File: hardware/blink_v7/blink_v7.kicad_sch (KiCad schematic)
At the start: 94 parts, among them J1 Conn_01x02, J14 Conn_02x16_Odd_Even, J5 Conn_01x04_Pin, J6 Conn_01x04_Pin, J7 Conn_01x06_Pin, J8 Conn_01x06, J9 USB_C_Receptacle, SW1 MK-12C02-G025, U1 AMS1117-3.3, U3 M24C02-RMN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

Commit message: start to add push button switch
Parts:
- added SW2, SW3, SW4: SW_SPDT, Button_Switch_THT:SW_Push_1P2T_Vertical_E-Switch_800UDP8P1A1M6, symbol Switch:SW_SPDT
- C27: JLCPCB Part # (none) -> C1525; JLCPCB# C1525 -> (none)
- C28, C29: JLCPCB Part # (none) -> C23733; JLCPCB# C23733 -> (none)
- D1: JLCPCB Part # (none) -> C130114; JLCPCB# C130114 -> (none)
- D2, D3: JLCPCB Part # (none) -> C191023; JLCPCB# C191023 -> (none)
- J9: JLCPCB Part # (none) -> C165948; JLCPCB# C165948 -> (none)
- R21, R22: JLCPCB Part # (none) -> C25905; JLCPCB# C25905 -> (none)
- R27: JLCPCB Part # C11702 -> C21190
- S1, S2: JLCPCB Part # (none) -> C266189
- U7: JLCPCB Part # (none) -> C84681; JLCPCB# C84681 -> (none)
- U8: JLCPCB Part # (none) -> C2827693; JLCPCB# C2827693 -> (none)
- U9: JLCPCB Part # (none) -> C424093; JLCPCB# C424093 -> (none)
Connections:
- net BTN1: now also SW2.2 (B)
- net GND: now also SW2.3 (C), SW3.3 (C), SW4.3 (C)

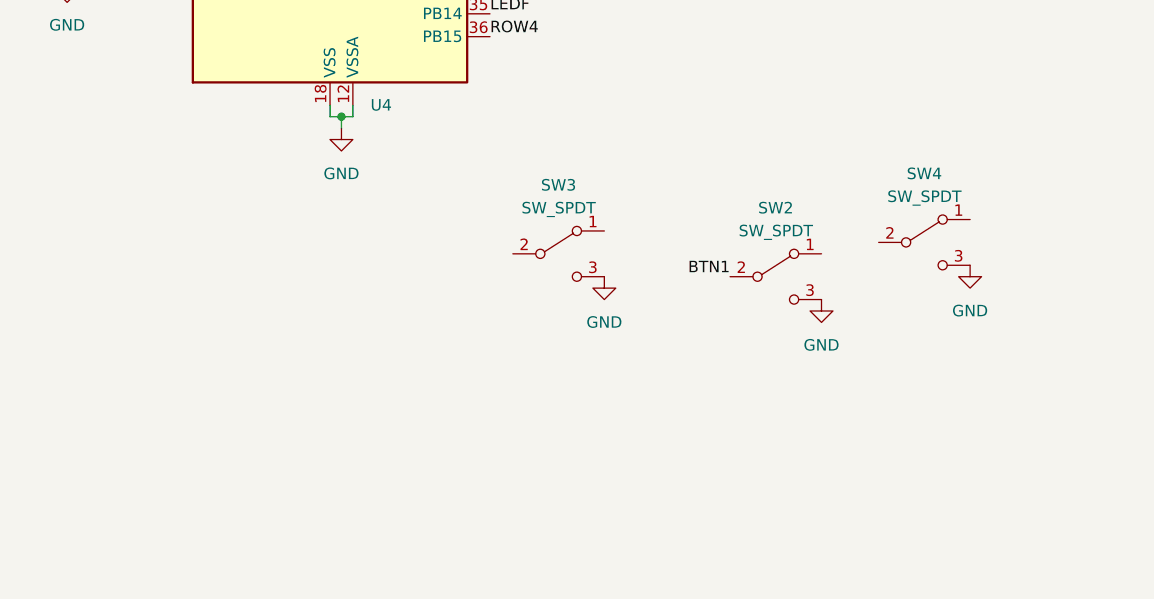
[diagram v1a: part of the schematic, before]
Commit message: wire up new switches
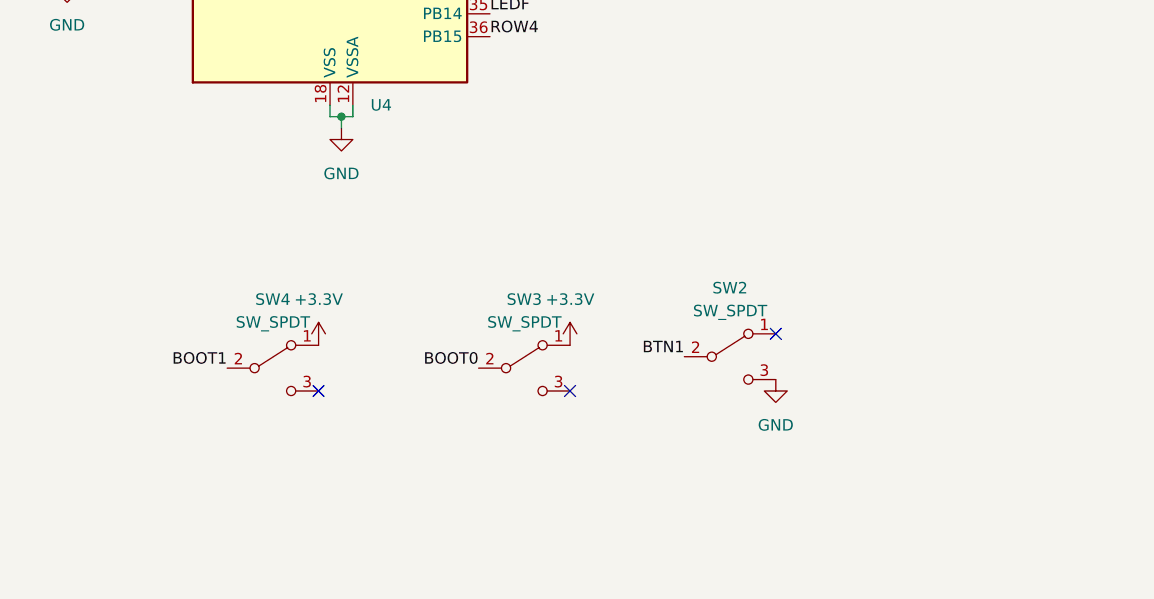
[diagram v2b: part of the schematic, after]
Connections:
- net +3.3V: now also SW3.1 (A), SW4.1 (A)
- net BOOT0: now also SW3.2 (B)
- net BOOT1: now also SW4.2 (B)
- net GND: no longer SW3.3 (C), SW4.3 (C)
- no-connect marks 21 -> 24
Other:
- moved on the sheet: SW2, SW3, SW4
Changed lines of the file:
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@@
   (junction (at 271.78 245.11) (diameter 0) (color 0 0 0 0)
   )
+  (no_connect (at 274.32 147.32))
   (no_connect (at 54.61 63.5))
   (no_connect (at 340.36 181.61))
+  (no_connect (at 223.52 153.67))
   (no_connect (at 389.89 184.15))
+  (no_connect (at 251.46 153.67))
   (no_connect (at 389.89 176.53))
   (no_connect (at 389.89 189.23))
@@
     (effects (font (size 1.27 1.27)) (justify left bottom))
   )
+  (label "BOOT0" (at 241.3 151.13 180) (fields_autoplaced)
+    (effects (font (size 1.27 1.27)) (justify right bottom))
+  )
   (label "SYNC_IN2" (at 207.01 71.12 180) (fields_autoplaced)
     (effects (font (size 1.27 1.27)) (justify right bottom))
@@
     (effects (font (size 1.27 1.27)) (justify left bottom))
   )
+  (label "BOOT1" (at 213.36 151.13 180) (fields_autoplaced)
+    (effects (font (size 1.27 1.27)) (justify right bottom))
+  )
   (label "USB_DTR" (at 309.88 196.85 0) (fields_autoplaced)
     (effects (font (size 1.27 1.27)) (justify left bottom))
@@
     (effects (font (size 1.27 1.27)) (justify left bottom))
   )
-  (label "BTN1" (at 269.24 140.97 180) (fields_autoplaced)
+  (label "BTN1" (at 264.16 149.86 180) (fields_autoplaced)
     (effects (font (size 1.27 1.27)) (justify right bottom))
   )
@@
     )
   )
-  (symbol (lib_id "Switch:SW_SPDT") (at 290.83 137.16 0) (unit 1)
+  (symbol (lib_id "Switch:SW_SPDT") (at 218.44 151.13 0) (unit 1)
     (in_bom yes) (on_board yes) (dnp no) (fields_autoplaced)
-    (property "Reference" "SW4" (at 290.83 129.54 0)
+    (property "Reference" "SW4" (at 218.44 143.51 0)
       (effects (font (size 1.27 1.27)))
     )
-    (property "Value" "SW_SPDT" (at 290.83 132.08 0)
+    (property "Value" "SW_SPDT" (at 218.44 146.05 0)
       (effects (font (size 1.27 1.27)))
     )
-    (property "Footprint" "Button_Switch_THT:SW_Push_1P2T_Vertical_E-Switch_800UDP8P1A1M6" (at 290.83 137.16 0)
+    (property "Footprint" "Button_Switch_THT:SW_Push_1P2T_Vertical_E-Switch_800UDP8P1A1M6" (at 218.44 151.13 0)
       (effects (font (size 1.27 1.27)) hide)
     )
-    (property "Datasheet" "~" (at 290.83 137.16 0)
+    (property "Datasheet" "~" (at 218.44 151.13 0)
       (effects (font (size 1.27 1.27)) hide)
     )
-    (property "JLCPCB Part #" "C273412" (at 290.83 137.16 0)
+    (property "JLCPCB Part #" "C273412" (at 218.44 151.13 0)
       (effects (font (size 1.27 1.27)) hide)
     )
@@
     )
   )
+  (symbol (lib_id "power:+3.3V") (at 223.52 148.59 0) (unit 1)
+    (in_bom yes) (on_board yes) (dnp no) (fields_autoplaced)
+    (property "Reference" "#PWR076" (at 223.52 152.4 0)
+      (effects (font (size 1.27 1.27)) hide)
+    )
+    (property "Value" "+3.3V" (at 223.52 143.51 0)
+      (effects (font (size 1.27 1.27)))
+    )
+    (property "Footprint" "" (at 223.52 148.59 0)
+      (effects (font (size 1.27 1.27)) hide)
+    )
+    (property "Datasheet" "" (at 223.52 148.59 0)
+      (effects (font (size 1.27 1.27)) hide)
+    )
+    (pin "1")
+    (instances
+      (project "blink_v7"
+        (path "/bd4d3b9a-07c1-4a53-9c94-2893f3e869d4"
+          (reference "#PWR076") (unit 1)
+        )
+      )
+    )
+  )
   (symbol (lib_id "Connector_Generic:Conn_01x06") (at 125.73 87.63 180) (unit 1)
     (in_bom yes) (on_board yes) (dnp no) (fields_autoplaced)
@@
     )
   )
-  (symbol (lib_id "power:GND") (at 279.4 143.51 0) (unit 1)
+  (symbol (lib_id "power:GND") (at 274.32 152.4 0) (unit 1)
     (in_bom yes) (on_board yes) (dnp no) (fields_autoplaced)
-    (property "Reference" "#PWR032" (at 279.4 149.86 0)
+    (property "Reference" "#PWR032" (at 274.32 158.75 0)
       (effects (font (size 1.27 1.27)) hide)
     )
-    (property "Value" "GND" (at 279.4 148.59 0)
+    (property "Value" "GND" (at 274.32 157.48 0)
       (effects (font (size 1.27 1.27)))
     )
-    (property "Footprint" "" (at 279.4 143.51 0)
+    (property "Footprint" "" (at 274.32 152.4 0)
       (effects (font (size 1.27 1.27)) hide)
     )
-    (property "Datasheet" "" (at 279.4 143.51 0)
+    (property "Datasheet" "" (at 274.32 152.4 0)
       (effects (font (size 1.27 1.27)) hide)
     )
@@
     )
   )
-  (symbol (lib_id "Switch:SW_SPDT") (at 250.19 138.43 0) (unit 1)
+  (symbol (lib_id "Switch:SW_SPDT") (at 246.38 151.13 0) (unit 1)
     (in_bom yes) (on_board yes) (dnp no) (fields_autoplaced)
-    (property "Reference" "SW3" (at 250.19 130.81 0)
+    (property "Reference" "SW3" (at 246.38 143.51 0)
       (effects (font (size 1.27 1.27)))
     )
-    (property "Value" "SW_SPDT" (at 250.19 133.35 0)
+    (property "Value" "SW_SPDT" (at 246.38 146.05 0)
       (effects (font (size 1.27 1.27)))
     )
-    (property "Footprint" "Button_Switch_THT:SW_Push_1P2T_Vertical_E-Switch_800UDP8P1A1M6" (at 250.19 138.43 0)
+    (property "Footprint" "Button_Switch_THT:SW_Push_1P2T_Vertical_E-Switch_800UDP8P1A1M6" (at 246.38 151.13 0)
       (effects (font (size 1.27 1.27)) hide)
     )
-    (property "Datasheet" "~" (at 250.19 138.43 0)
+    (property "Datasheet" "~" (at 246.38 151.13 0)
       (effects (font (size 1.27 1.27)) hide)
     )
-    (property "JLCPCB Part #" "C273412" (at 250.19 138.43 0)
+    (property "JLCPCB Part #" "C273412" (at 246.38 151.13 0)
       (effects (font (size 1.27 1.27)) hide)
     )
@@
     )
   )
+  (symbol (lib_id "power:+3.3V") (at 251.46 148.59 0) (unit 1)
+    (in_bom yes) (on_board yes) (dnp no) (fields_autoplaced)
+    (property "Reference" "#PWR077" (at 251.46 152.4 0)
+      (effects (font (size 1.27 1.27)) hide)
+    )
+    (property "Value" "+3.3V" (at 251.46 143.51 0)
+      (effects (font (size 1.27 1.27)))
+    )
+    (property "Footprint" "" (at 251.46 148.59 0)
+      (effects (font (size 1.27 1.27)) hide)
+    )
+    (property "Datasheet" "" (at 251.46 148.59 0)
+      (effects (font (size 1.27 1.27)) hide)
+    )
+    (pin "1")
+    (instances
+      (project "blink_v7"
+        (path "/bd4d3b9a-07c1-4a53-9c94-2893f3e869d4"
+          (reference "#PWR077") (unit 1)
+        )
+      )
+    )
+  )
   (symbol (lib_id "Device:C") (at 326.39 166.37 0) (mirror y) (unit 1)
     (in_bom yes) (on_board yes) (dnp no)
@@
     )
   )
-  (symbol (lib_id "power:GND") (at 295.91 139.7 0) (unit 1)
-    (in_bom yes) (on_board yes) (dnp no) (fields_autoplaced)
-    (property "Reference" "#PWR075" (at 295.91 146.05 0)
-      (effects (font (size 1.27 1.27)) hide)
-    )
-    (property "Value" "GND" (at 295.91 144.78 0)
-      (effects (font (size 1.27 1.27)))
-    )
-    (property "Footprint" "" (at 295.91 139.7 0)
-      (effects (font (size 1.27 1.27)) hide)
-    )
-    (property "Datasheet" "" (at 295.91 139.7 0)
-      (effects (font (size 1.27 1.27)) hide)
-    )
-    (pin "1")
-    (instances
-      (project "blink_v7"
-        (path "/bd4d3b9a-07c1-4a53-9c94-2893f3e869d4"
-          (reference "#PWR075") (unit 1)
-        )
-      )
-    )
-  )
   (symbol (lib_id "Device:R_Small_US") (at 323.85 105.41 0) (unit 1)
     (in_bom yes) (on_board yes) (dnp no)
@@
     )
   )
-  (symbol (lib_id "Switch:SW_SPDT") (at 274.32 140.97 0) (unit 1)
+  (symbol (lib_id "Switch:SW_SPDT") (at 269.24 149.86 0) (unit 1)
     (in_bom yes) (on_board yes) (dnp no) (fields_autoplaced)
-    (property "Reference" "SW2" (at 274.32 133.35 0)
+    (property "Reference" "SW2" (at 269.24 142.24 0)
       (effects (font (size 1.27 1.27)))
     )
-    (property "Value" "SW_SPDT" (at 274.32 135.89 0)
+    (property "Value" "SW_SPDT" (at 269.24 144.78 0)
       (effects (font (size 1.27 1.27)))
     )
-    (property "Footprint" "Button_Switch_THT:SW_Push_1P2T_Vertical_E-Switch_800UDP8P1A1M6" (at 274.32 140.97 0)
+    (property "Footprint" "Button_Switch_THT:SW_Push_1P2T_Vertical_E-Switch_800UDP8P1A1M6" (at 269.24 149.86 0)
       (effects (font (size 1.27 1.27)) hide)
     )
-    (property "Datasheet" "~" (at 274.32 140.97 0)
+    (property "Datasheet" "~" (at 269.24 149.86 0)
       (effects (font (size 1.27 1.27)) hide)
     )
-    (property "JLCPCB Part #" "C273412" (at 274.32 140.97 0)
+    (property "JLCPCB Part #" "C273412" (at 269.24 149.86 0)
       (effects (font (size 1.27 1.27)) hide)
     )
@@
         )
       )
-    )
-  )
-  (symbol (lib_id "power:GND") (at 255.27 140.97 0) (unit 1)
-    (in_bom yes) (on_board yes) (dnp no) (fields_autoplaced)
-    (property "Reference" "#PWR04" (at 255.27 147.32 0)
-      (effects (font (size 1.27 1.27)) hide)
-    )
-    (property "Value" "GND" (at 255.27 146.05 0)
-      (effects (font (size 1.27 1.27)))
-    )
-    (property "Footprint" "" (at 255.27 140.97 0)
-      (effects (font (size 1.27 1.27)) hide)
-    )
-    (property "Datasheet" "" (at 255.27 140.97 0)
-      (effects (font (size 1.27 1.27)) hide)
-    )
-    (pin "1")
-    (instances
-      (project "blink_v7"
-        (path "/bd4d3b9a-07c1-4a53-9c94-2893f3e869d4"
-          (reference "#PWR04") (unit 1)
-        )
-      )

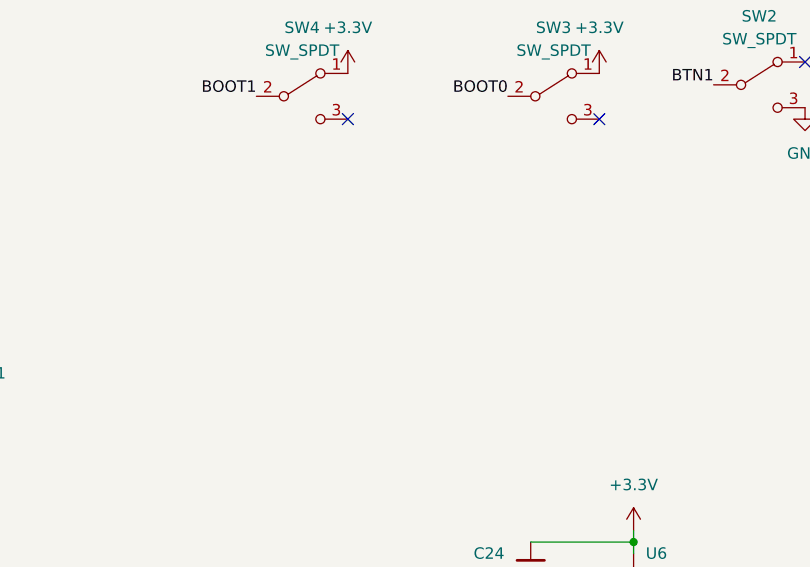
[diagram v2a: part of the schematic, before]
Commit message: start moving to new push switch
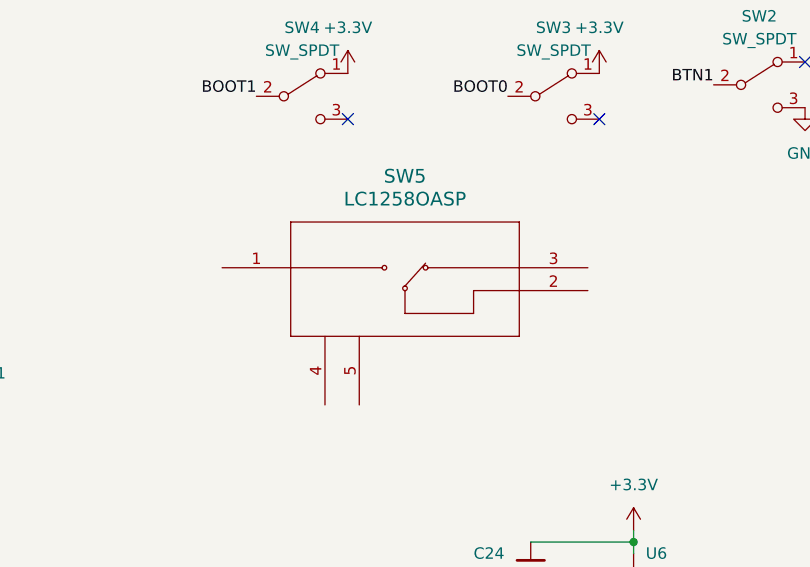
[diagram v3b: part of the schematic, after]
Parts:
- added SW5: LC1258OASP, blinky_footprints:LC1258OASP, symbol blinky:LC1258OASP
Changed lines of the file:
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@@
+    )
+  )
+  (symbol (lib_id "blinky:LC1258OASP") (at 209.55 170.18 0) (unit 1)
+    (in_bom yes) (on_board yes) (dnp no) (fields_autoplaced)
+    (property "Reference" "SW5" (at 229.87 160.02 0)
+      (effects (font (size 1.524 1.524)))
+    )
+    (property "Value" "LC1258OASP" (at 229.87 162.56 0)
+      (effects (font (size 1.524 1.524)))
+    )
+    (property "Footprint" "blinky_footprints:LC1258OASP" (at 229.87 176.53 0)
+      (effects (font (size 1.27 1.27) italic) hide)
+    )
+    (property "Datasheet" "" (at 209.55 170.18 0)
+      (effects (font (size 1.27 1.27) italic) hide)
+    )
+    (pin "1")
+    (pin "3")
+    (pin "4")
+    (pin "5")
+    (pin "2")
+    (instances
+      (project "blink_v7"
+        (path "/bd4d3b9a-07c1-4a53-9c94-2893f3e869d4"
+          (reference "SW5") (unit 1)
+        )
+      )
     )
   )

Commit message: update
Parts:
- SW2, SW3, SW4: footprint Button_Switch_THT:SW_Push_1P2T_Vertical_E-Switch_800UDP8P1A1M6 -> (none); JLCPCB Part # C273412 -> (none)
- SW5: JLCPCB Part # (none) -> C273412
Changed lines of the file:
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@@
       (effects (font (size 1.27 1.27)))
     )
-    (property "Footprint" "Button_Switch_THT:SW_Push_1P2T_Vertical_E-Switch_800UDP8P1A1M6" (at 218.44 151.13 0)
+    (property "Footprint" "" (at 218.44 151.13 0)
       (effects (font (size 1.27 1.27)) hide)
     )
@@
       (effects (font (size 1.27 1.27)) hide)
     )
-    (property "JLCPCB Part #" "C273412" (at 218.44 151.13 0)
+    (property "JLCPCB Part #" "" (at 218.44 151.13 0)
       (effects (font (size 1.27 1.27)) hide)
     )
@@
       (effects (font (size 1.27 1.27)))
     )
-    (property "Footprint" "Button_Switch_THT:SW_Push_1P2T_Vertical_E-Switch_800UDP8P1A1M6" (at 246.38 151.13 0)
+    (property "Footprint" "" (at 246.38 151.13 0)
       (effects (font (size 1.27 1.27)) hide)
     )
@@
       (effects (font (size 1.27 1.27)) hide)
     )
-    (property "JLCPCB Part #" "C273412" (at 246.38 151.13 0)
+    (property "JLCPCB Part #" "" (at 246.38 151.13 0)
       (effects (font (size 1.27 1.27)) hide)
     )
@@
       (effects (font (size 1.27 1.27) italic) hide)
     )
-    (property "Datasheet" "" (at 209.55 170.18 0)
+    (property "Datasheet" "https://sten-eswitch-13110800-production.s3.amazonaws.com/system/asset/product_line/data_sheet/36/LC.pdf" (at 209.55 170.18 0)
       (effects (font (size 1.27 1.27) italic) hide)
+    )
+    (property "JLCPCB Part #" "C273412" (at 209.55 170.18 0)
+      (effects (font (size 1.27 1.27)) hide)
     )
     (pin "1")
@@
       (effects (font (size 1.27 1.27)))
     )
-    (property "Footprint" "Button_Switch_THT:SW_Push_1P2T_Vertical_E-Switch_800UDP8P1A1M6" (at 269.24 149.86 0)
+    (property "Footprint" "" (at 269.24 149.86 0)
       (effects (font (size 1.27 1.27)) hide)
     )
@@
       (effects (font (size 1.27 1.27)) hide)
     )
-    (property "JLCPCB Part #" "C273412" (at 269.24 149.86 0)
-      (effects (font (size 1.27 1.27)) hide)
-    )
+    (property "JLCPCB Part #" "" (at 269.24 149.86 0)
+      (effects (font (size 1.27 1.27)) hide)
+    )
